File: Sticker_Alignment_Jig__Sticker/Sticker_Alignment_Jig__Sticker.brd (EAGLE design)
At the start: 200 x 100 mm, 21 parts

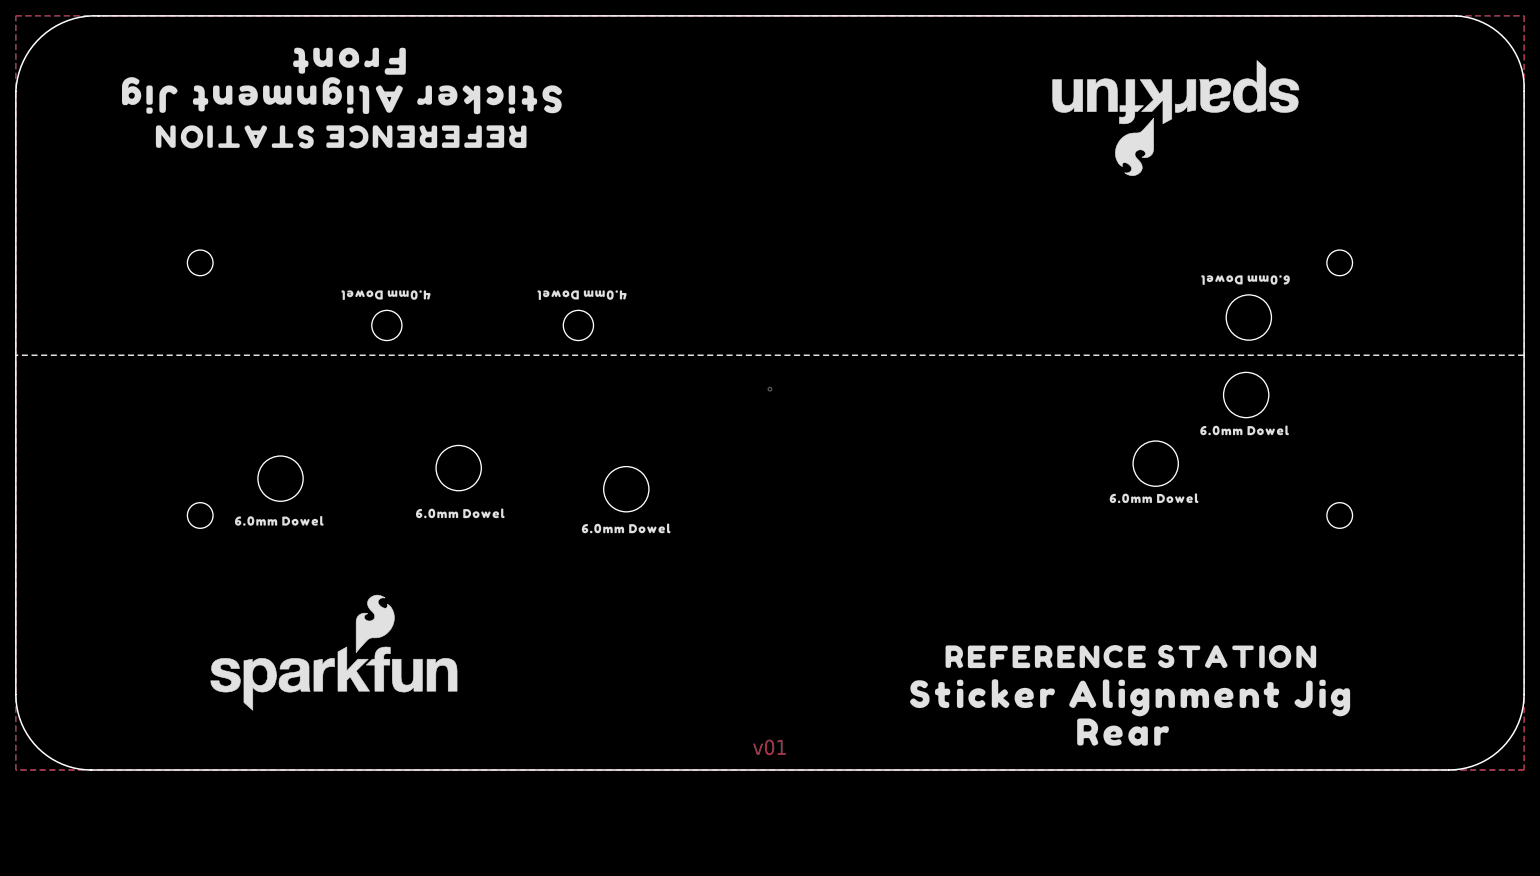
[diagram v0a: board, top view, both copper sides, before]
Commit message: Update sticker alignment jig
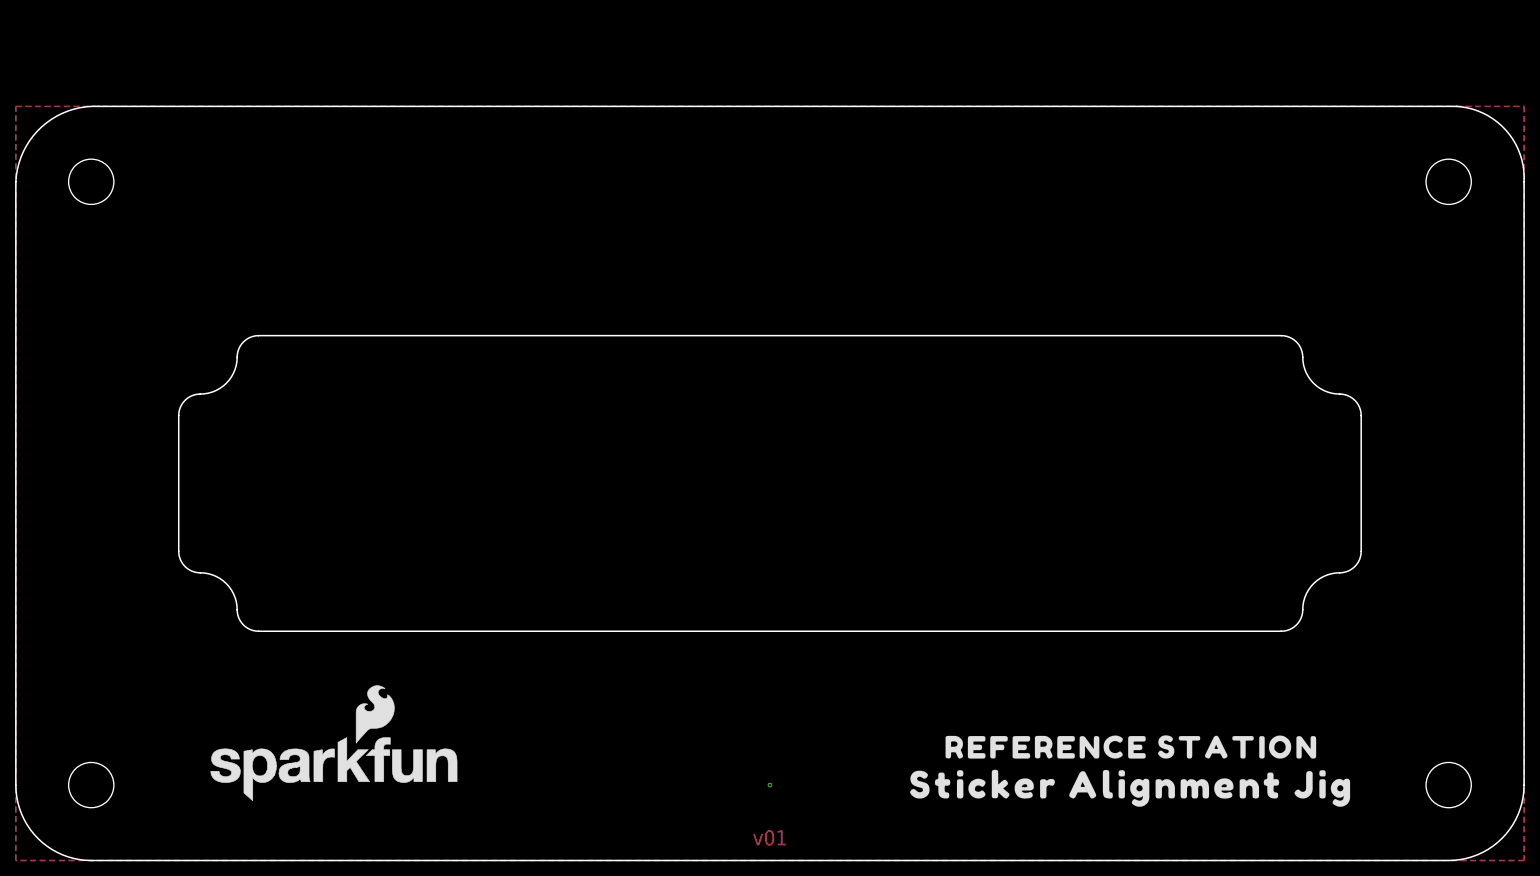
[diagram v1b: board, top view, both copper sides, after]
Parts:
- removed LOGO2: SFE_LOGO_NAME_FLAME.3_INCH, SparkFun-Aesthetics:SFE_LOGO_NAME_FLAME_.3
- removed U$10: (no value), output:STICKER_ALIGNMENT_JIG0
- removed U$11, U$19, U$20, U$6, U$7, U$8: (no value), output:6#0MM_DOWEL0
- removed U$12, U$4: (no value), output:4#0MM_DOWEL0
- removed U$13, U$14: BUTTON, CORS_Panels:BUTTON
- removed U$2: PANEL_OUTLINE, CORS_Panels:PANEL_OUTLINE
- removed U$21: (no value), output:FRONT0
- removed U$22: (no value), output:REAR0
- removed U$3: LED, CORS_Panels:LED
- removed U$9: (no value), output:REFERENCE_STATION0
- moved FRAME1 12.0 mm to (-25.0, -59.0)
- moved U$1 12.0 mm to (48.0, -35.0)
- moved U$5 12.0 mm to (48.0, -40.0)
- moved LOGO1 12.0 mm to (-57.9, -37.9)
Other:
- outline, holes or cut-outs redrawn
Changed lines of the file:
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@@
 <drawing>
 <settings>
-<setting alwaysvectorfont="yes"/>
+<setting alwaysvectorfont="no"/>
 <setting verticaltext="up"/>
 </settings>
@@
 <board>
 <plain>
-<wire x1="-100" y1="-28" x2="-90" y2="-38" width="0.2" layer="20" curve="90"/>
-<wire x1="-90" y1="-38" x2="90" y2="-38" width="0.2" layer="20"/>
-<wire x1="90" y1="-38" x2="100" y2="-28" width="0.2" layer="20" curve="90"/>
-<wire x1="100" y1="-28" x2="100" y2="52" width="0.2" layer="20"/>
-<wire x1="100" y1="52" x2="91" y2="62" width="0.2" layer="20" curve="90"/>
-<wire x1="91" y1="62" x2="-89" y2="62" width="0.2" layer="20"/>
-<wire x1="-89" y1="62" x2="-100" y2="52" width="0.2" layer="20" curve="90"/>
-<wire x1="-100" y1="52" x2="-100" y2="-28" width="0.2" layer="20"/>
-<text x="0" y="-36" size="2" layer="1" font="vector" ratio="15" align="bottom-center">v01</text>
-<hole x="51.15" y="2.625" drill="6"/>
-<hole x="63.15" y="11.725" drill="6"/>
-<hole x="-64.9" y="0.635" drill="6"/>
-<wire x1="79.3" y1="0" x2="-79.3" y2="0" width="0.2" layer="51" style="dashdot"/>
-<hole x="-41.275" y="2.035" drill="6"/>
-<hole x="-19.05" y="-0.765" drill="6"/>
-<wire x1="100" y1="17" x2="-100" y2="17" width="0.2" layer="21" style="dashdot"/>
+<wire x1="-100" y1="-40" x2="-90" y2="-50" width="0.2" layer="20" curve="90"/>
+<wire x1="-90" y1="-50" x2="90" y2="-50" width="0.2" layer="20"/>
+<wire x1="90" y1="-50" x2="100" y2="-40" width="0.2" layer="20" curve="90"/>
+<wire x1="100" y1="-40" x2="100" y2="40" width="0.2" layer="20"/>
+<wire x1="100" y1="40" x2="91" y2="50" width="0.2" layer="20" curve="90"/>
+<wire x1="91" y1="50" x2="-89" y2="50" width="0.2" layer="20"/>
+<wire x1="-89" y1="50" x2="-100" y2="40" width="0.2" layer="20" curve="90"/>
+<wire x1="-100" y1="40" x2="-100" y2="-40" width="0.2" layer="20"/>
+<text x="0" y="-48" size="2" layer="1" font="vector" ratio="15" align="bottom-center">v01</text>
+<wire x1="-78.4" y1="9" x2="-78.4" y2="-9" width="0.2" layer="20"/>
+<wire x1="-67.8" y1="-19.6" x2="67.8" y2="-19.6" width="0.2" layer="20"/>
+<wire x1="78.4" y1="-9" x2="78.4" y2="9" width="0.2" layer="20"/>
+<wire x1="67.8" y1="19.6" x2="-67.8" y2="19.6" width="0.2" layer="20"/>
+<wire x1="70.65" y1="-16.75" x2="75.55" y2="-11.85" width="0.2" layer="20" curve="-90"/>
+<wire x1="70.65" y1="-16.75" x2="67.8" y2="-19.6" width="0.2" layer="20" curve="-90"/>
+<wire x1="78.4" y1="-9" x2="75.55" y2="-11.85" width="0.2" layer="20" curve="-90"/>
+<wire x1="75.55" y1="11.85" x2="70.65" y2="16.75" width="0.2" layer="20" curve="-90"/>
+<wire x1="75.55" y1="11.85" x2="78.4" y2="9" width="0.2" layer="20" curve="-90"/>
+<wire x1="67.8" y1="19.6" x2="70.65" y2="16.75" width="0.2" layer="20" curve="-90"/>
+<wire x1="-70.65" y1="16.75" x2="-75.55" y2="11.85" width="0.2" layer="20" curve="-90"/>
+<wire x1="-70.65" y1="16.75" x2="-67.8" y2="19.6" width="0.2" layer="20" curve="-90"/>
+<wire x1="-78.4" y1="9" x2="-75.55" y2="11.85" width="0.2" layer="20" curve="-90"/>
+<wire x1="-75.55" y1="-11.85" x2="-70.65" y2="-16.75" width="0.2" layer="20" curve="-90"/>
+<wire x1="-75.55" y1="-11.85" x2="-78.4" y2="-9" width="0.2" layer="20" curve="-90"/>
+<wire x1="-67.8" y1="-19.6" x2="-70.65" y2="-16.75" width="0.2" layer="20" curve="-90"/>
+<hole x="-90" y="40" drill="6"/>
+<hole x="90" y="40" drill="6"/>
+<hole x="90" y="-40" drill="6"/>
+<hole x="-90" y="-40" drill="6"/>
 </plain>
 <attributes>
@@
 </autorouter>
 <elements>
-<element name="LOGO1" library="SparkFun-Aesthetics" package="SFE_LOGO_NAME_FLAME_.3" value="SFE_LOGO_NAME_FLAME.3_INCH" x="-57.8504" y="-25.9111" smashed="yes"/>
-<element name="U$1" library="output" package="REFERENCE_STATION0" value="" x="48" y="-23" smashed="yes"/>
-<element name="FRAME1" library="SparkFun-Aesthetics" package="CREATIVE_COMMONS" value="FRAME-LETTER" x="-25" y="-47" smashed="yes">
-<attribute name="DESIGNER" value="" x="-25" y="-47" size="1.778" layer="27" ratio="15" display="off"/>
-<attribute name="REV" value="" x="-25" y="-47" size="1.778" layer="27" ratio="15" display="off"/>
+<element name="LOGO1" library="SparkFun-Aesthetics" package="SFE_LOGO_NAME_FLAME_.3" value="SFE_LOGO_NAME_FLAME.3_INCH" x="-57.8504" y="-37.9111" smashed="yes"/>
+<element name="U$1" library="output" package="REFERENCE_STATION0" value="" x="48" y="-35" smashed="yes"/>
+<element name="FRAME1" library="SparkFun-Aesthetics" package="CREATIVE_COMMONS" value="FRAME-LETTER" x="-25" y="-59" smashed="yes">
+<attribute name="DESIGNER" value="" x="-25" y="-59" size="1.778" layer="27" ratio="15" display="off"/>
+<attribute name="REV" value="" x="-25" y="-59" size="1.778" layer="27" ratio="15" display="off"/>
 </element>
-<element name="U$6" library="output" package="6#0MM_DOWEL0" value="" x="63" y="7" smashed="yes"/>
-<element name="U$7" library="output" package="6#0MM_DOWEL0" value="" x="51" y="-2" smashed="yes"/>
-<element name="U$8" library="output" package="6#0MM_DOWEL0" value="" x="-65" y="-5" smashed="yes"/>
-<element name="U$11" library="output" package="6#0MM_DOWEL0" value="" x="63" y="27" smashed="yes" rot="R180"/>
-<element name="U$5" library="output" package="STICKER_ALIGNMENT_JIG0" value="" x="48" y="-28" smashed="yes"/>
-<element name="U$2" library="CORS_Panels" package="PANEL_OUTLINE" value="PANEL_OUTLINE" x="0" y="25" smashed="yes" rot="R180"/>
-<element name="U$3" library="CORS_Panels" package="LED" value="LED" x="63.5" y="25" smashed="yes" rot="R180"/>
-<element name="LOGO2" library="SparkFun-Aesthetics" package="SFE_LOGO_NAME_FLAME_.3" value="SFE_LOGO_NAME_FLAME.3_INCH" x="53.8504" y="51.9111" smashed="yes" rot="R180"/>
-<element name="U$9" library="output" package="REFERENCE_STATION0" value="" x="-57" y="46" smashed="yes" rot="R180"/>
-<element name="U$10" library="output" package="STICKER_ALIGNMENT_JIG0" value="" x="-57" y="51" smashed="yes" rot="R180"/>
-<element name="U$13" library="CORS_Panels" package="BUTTON" value="BUTTON" x="-50.8" y="25" smashed="yes" rot="R180"/>
-<element name="U$14" library="CORS_Panels" package="BUTTON" value="BUTTON" x="-25.4" y="25" smashed="yes" rot="R180"/>
-<element name="U$4" library="output" package="4#0MM_DOWEL0" value="" x="-25" y="25" smashed="yes" rot="R180"/>
-<element name="U$12" library="output" package="4#0MM_DOWEL0" value="" x="-51" y="25" smashed="yes" rot="R180"/>
-<element name="U$19" library="output" package="6#0MM_DOWEL0" value="" x="-41" y="-4" smashed="yes"/>
-<element name="U$20" library="output" package="6#0MM_DOWEL0" value="" x="-19" y="-6" smashed="yes"/>
-<element name="U$21" library="output" package="FRONT0" value="" x="-56" y="56" smashed="yes" rot="R180"/>
-<element name="U$22" library="output" package="REAR0" value="" x="47" y="-33" smashed="yes"/>
+<element name="U$5" library="output" package="STICKER_ALIGNMENT_JIG0" value="" x="48" y="-40" smashed="yes"/>
 </elements>
 <signals>
 <signal name="GND">
 <polygon width="0.2" layer="1" isolate="0.5" thermals="no">
-<vertex x="-100" y="62"/>
-<vertex x="100" y="62"/>
-<vertex x="100" y="-38"/>
-<vertex x="-100" y="-38"/>
+<vertex x="-100" y="50"/>
+<vertex x="100" y="50"/>
+<vertex x="100" y="-50"/>
+<vertex x="-100" y="-50"/>
 </polygon>
 <polygon width="0.2" layer="16" isolate="0.5" thermals="no">
-<vertex x="-100" y="62"/>
-<vertex x="100" y="62"/>
-<vertex x="100" y="-38"/>
-<vertex x="-100" y="-38"/>
+<vertex x="-100" y="50"/>
+<vertex x="100" y="50"/>
+<vertex x="100" y="-50"/>
+<vertex x="-100" y="-50"/>
 </polygon>
-<via x="0" y="12.5" extent="1-16" drill="0.3"/>
+<via x="0" y="-40" extent="1-16" drill="0.3"/>
 </signal>
 </signals>
